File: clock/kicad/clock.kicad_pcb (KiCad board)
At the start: 2 copper layers, 152.9 x 74.9 mm, 75 parts, among them J1 USB-SS-52100-001, Q1 PN2222A, SW1 HOUR, SW2 MIN, SW3 TIME, U1 74HC4060, U10 74HC390, U11 NE555P, U12 74HC4511, U13 74HC4511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

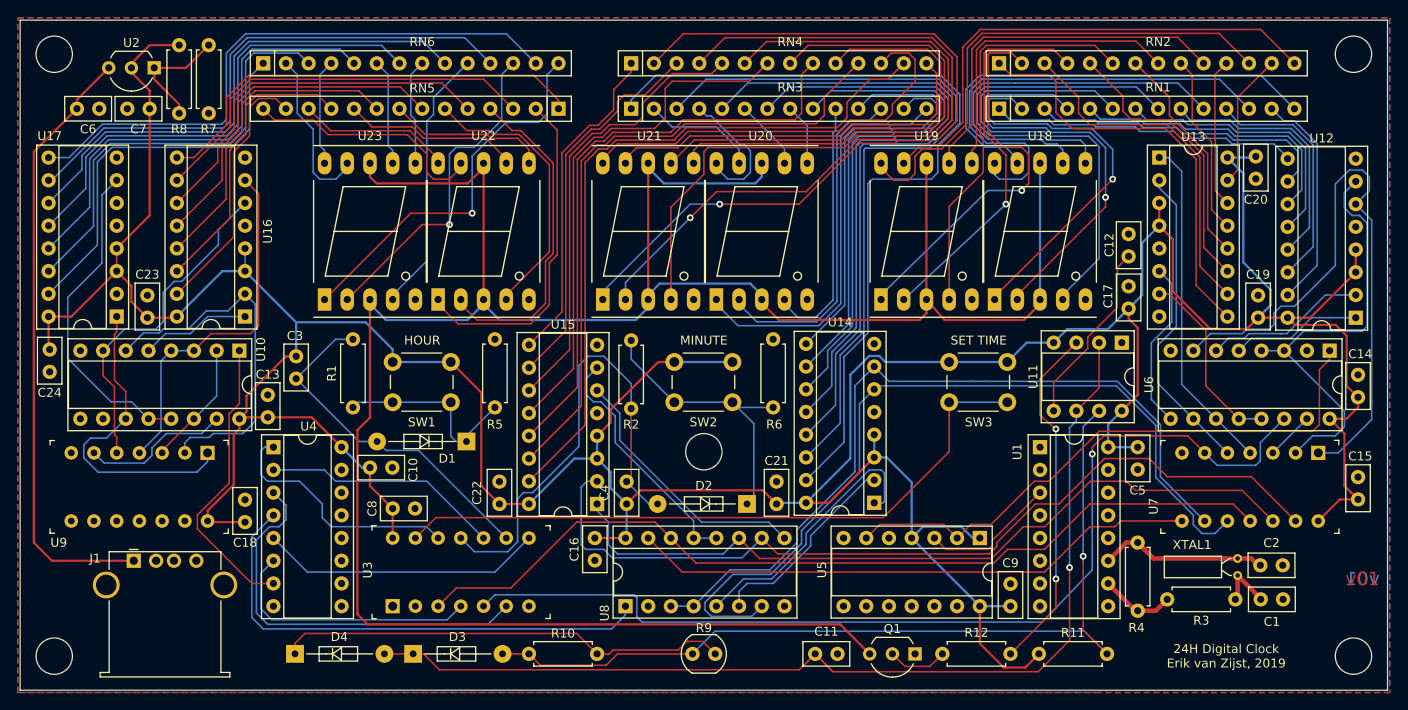
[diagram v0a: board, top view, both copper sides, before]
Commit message: Clock: Using a 500Ohm trimpot to tune the voltage regulator.
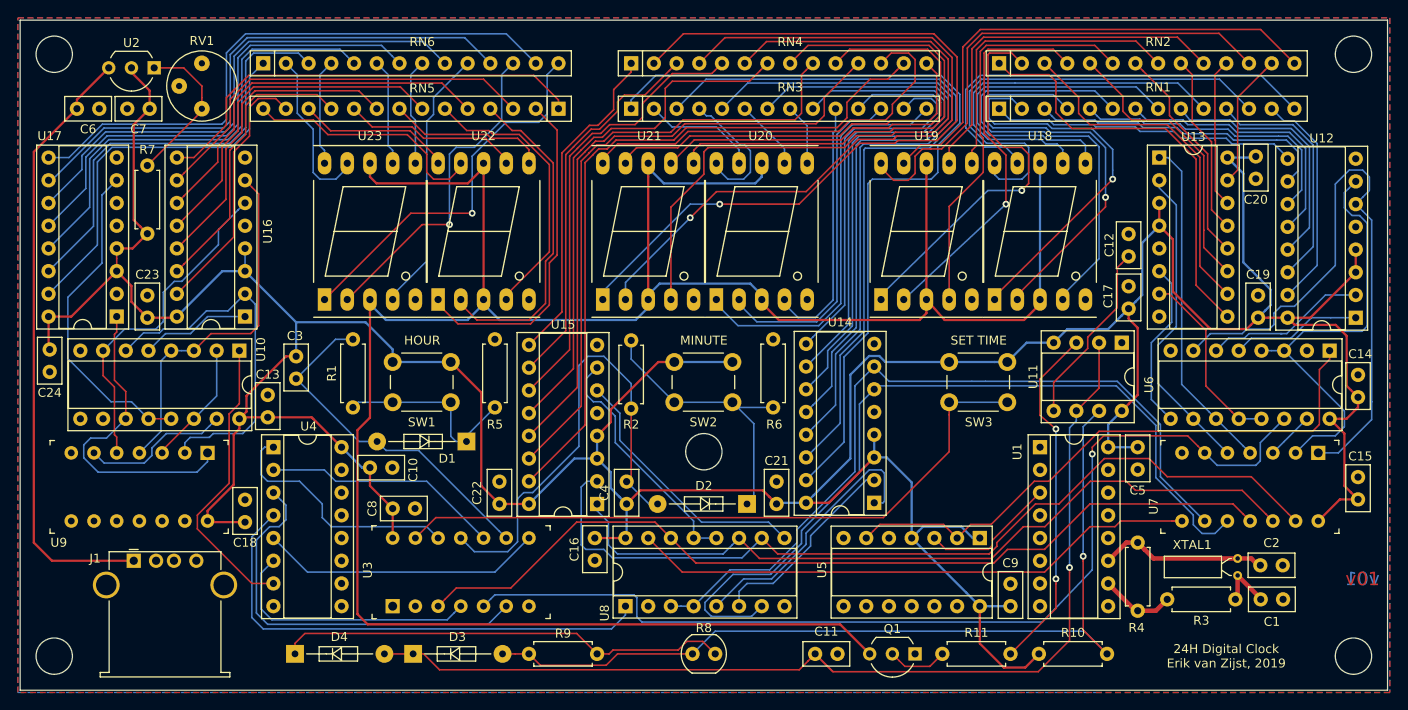
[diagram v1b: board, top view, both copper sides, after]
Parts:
- removed the R7 at (145.3, 59.9)
- added RV1: 0-500, Potentiometer_THT:Potentiometer_Bourns_3339P_Vertical_HandSoldering, F.Cu at (144.5, 67.1)
- moved R7 21.4 mm to (138.4, 81.0), turned to 90 degrees
- renumbered R11 to R10, R12 to R11, R8 to R7, R9 to R8, R10 to R9
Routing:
- net VCC: track 479.6 -> 475.2 mm
- net Net-(R7-Pad2): track 13.4 -> 17.6 mm

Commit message: Clock: Tweak PWM RC values.
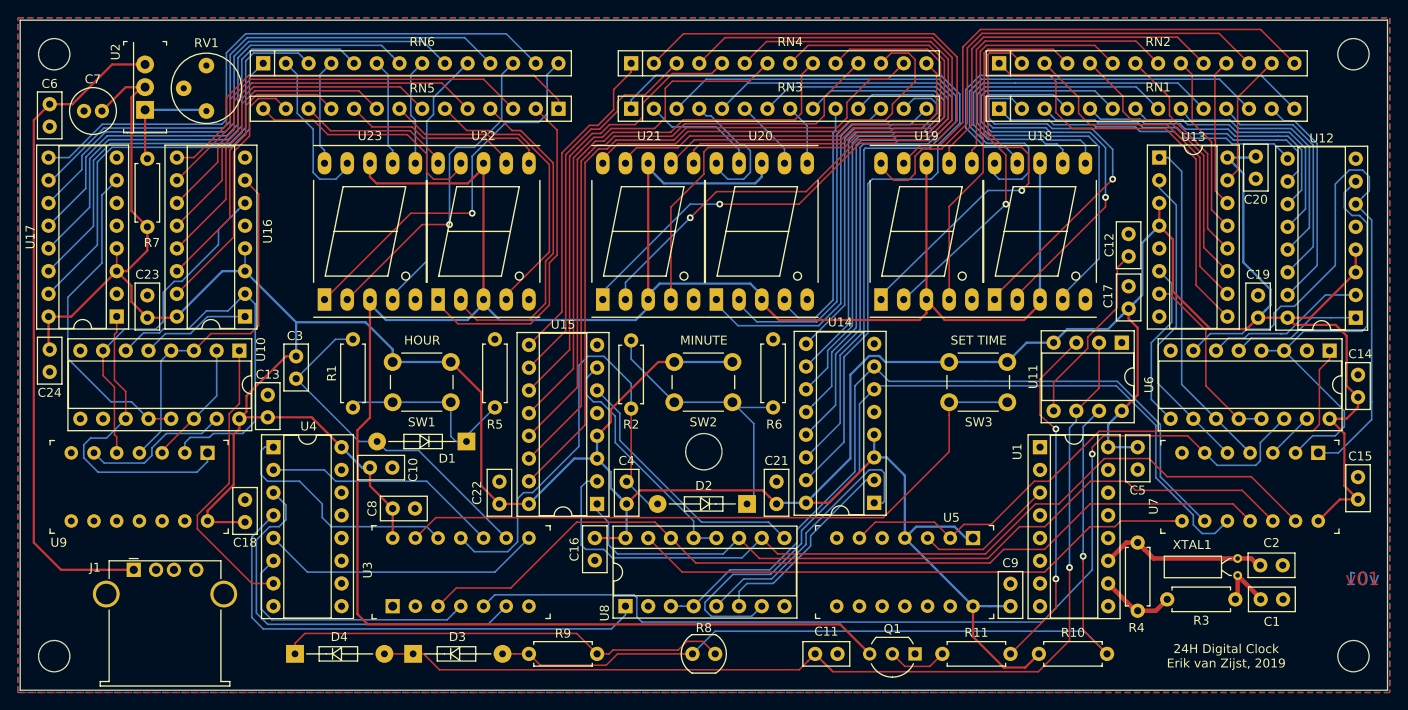
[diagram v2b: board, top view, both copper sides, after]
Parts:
- C7: footprint Capacitor_THT:C_Disc_D5.0mm_W2.5mm_P2.50mm -> Capacitor_THT:C_Radial_D5.0mm_H11.0mm_P2.00mm
- R7: value 120 -> 220
- U2: value LM317L_TO92 -> LD1117V; footprint Package_TO_SOT_THT:TO-92_Inline_Wide -> digikey-footprints:TO-220-3
- U5: footprint Package_DIP:DIP-14_W7.62mm_Socket -> clock:Socket_DIP-14_0.775in_Conn
- moved C7 5.34 mm to (133.3, 67.3)
- moved U2 4.81 mm to (138.2, 67.2), turned to 90 degrees
- moved C6 3.09 mm to (127.5, 66.5), turned to 270 degrees
- moved J1 1.02 mm to (136.9, 118.6)
- moved R7 0.76 mm to (138.4, 80.3)
- moved U5 0.76 mm to (230.8, 115.1)
- moved RV1 0.57 mm to (145.0, 67.3)
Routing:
- net /5V: track 68.6 -> 74.7 mm
- net VCC: track 475.2 -> 481.3 mm
- net Net-(R7-Pad2): track 17.6 -> 12.5 mm
- net Net-(U5-Pad2): track 65.9 -> 66.9 mm
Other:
- outline, holes or cut-outs redrawn

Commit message: Clock: Changed Resistor Networks to real parts.
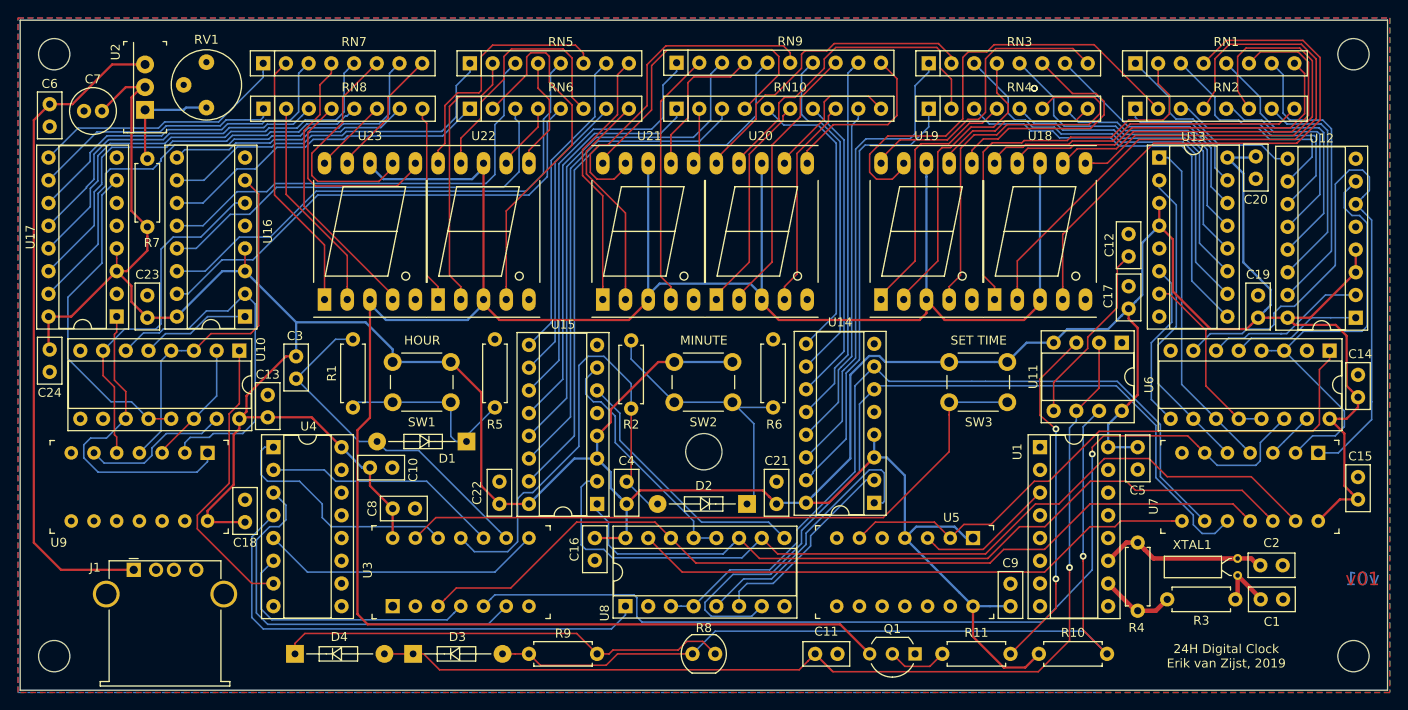
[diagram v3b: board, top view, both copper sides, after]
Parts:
- added RN10: R_Pack05_SIP, Resistor_THT:R_Array_SIP10, F.Cu at (197.6, 67.1)
- added RN7: R_Pack04_SIP, Resistor_THT:R_Array_SIP8, F.Cu at (151.4, 62.0)
- added RN8: R_Pack04_SIP, Resistor_THT:R_Array_SIP8, F.Cu at (151.4, 67.1)
- added RN9: R_Pack05_SIP, Resistor_THT:R_Array_SIP10, F.Cu at (197.6, 61.9)
- C11: value 100nF -> 47nF
- R10: value 1K -> 10K
- R11: value 100K -> 5.1K
- R9: value 100K -> 1M
- RN1, RN2, RN3, RN4, RN5, RN6: value 330 -> R_Pack04_SIP; footprint Resistor_THT:R_Array_SIP14 -> Resistor_THT:R_Array_SIP8
- moved RN3 33.7 mm to (225.8, 62.0)
- moved RN4 33.7 mm to (225.8, 67.1)
- moved RN6 23.7 mm to (174.5, 67.1)
- moved RN1 16.1 mm to (248.9, 62.0)
- moved RN2 16.1 mm to (248.9, 67.1)
- moved RN5 11.1 mm to (174.5, 62.0), turned to 0 degrees
- moved RV1 0.38 mm to (145.0, 66.9)
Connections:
- U12 pad 10: Net-(RN1-Pad3) -> Net-(RN2-Pad3)
- U12 pad 11: Net-(RN1-Pad5) -> Net-(RN1-Pad3)
- U12 pad 12: Net-(RN1-Pad7) -> Net-(RN2-Pad5)
- U12 pad 13: Net-(RN1-Pad9) -> Net-(RN1-Pad5)
- U12 pad 14: Net-(RN1-Pad11) -> Net-(RN2-Pad7)
- U12 pad 15: Net-(RN1-Pad13) -> Net-(RN1-Pad7)
- U13 pad 10: Net-(RN2-Pad3) -> Net-(RN3-Pad3)
- U13 pad 11: Net-(RN2-Pad5) -> Net-(RN4-Pad5)
- U13 pad 12: Net-(RN2-Pad7) -> Net-(RN3-Pad5)
- U13 pad 13: Net-(RN2-Pad9) -> Net-(RN4-Pad7)
- U13 pad 14: Net-(RN2-Pad11) -> Net-(RN3-Pad7)
- U13 pad 15: Net-(RN2-Pad13) -> Net-(RN2-Pad1)
- U13 pad 9: Net-(RN2-Pad1) -> Net-(RN4-Pad3)
- U14 pad 10: Net-(RN3-Pad11) -> Net-(RN9-Pad7)
- U14 pad 11: Net-(RN3-Pad9) -> Net-(RN10-Pad7)
- U14 pad 12: Net-(RN3-Pad7) -> Net-(RN9-Pad9)
- U14 pad 13: Net-(RN3-Pad5) -> Net-(RN10-Pad9)
- U14 pad 14: Net-(RN3-Pad3) -> Net-(RN3-Pad1)
- U14 pad 15: Net-(RN3-Pad1) -> Net-(RN4-Pad1)
- U14 pad 9: Net-(RN3-Pad13) -> Net-(RN10-Pad5)
- U15 pad 10: Net-(RN4-Pad3) -> Net-(RN6-Pad7)
- U15 pad 11: Net-(RN4-Pad5) -> Net-(RN9-Pad1)
- U15 pad 12: Net-(RN4-Pad7) -> Net-(RN10-Pad1)
- U15 pad 13: Net-(RN4-Pad9) -> Net-(RN9-Pad3)
- U15 pad 14: Net-(RN4-Pad11) -> Net-(RN10-Pad3)
- U15 pad 15: Net-(RN4-Pad13) -> Net-(RN9-Pad5)
- U15 pad 9: Net-(RN4-Pad1) -> Net-(RN5-Pad7)
- U16 pad 10: Net-(RN5-Pad3) -> Net-(RN5-Pad1)
- U16 pad 11: Net-(RN5-Pad5) -> Net-(RN6-Pad1)
- U16 pad 12: Net-(RN5-Pad7) -> Net-(RN5-Pad3)
- U16 pad 13: Net-(RN5-Pad9) -> Net-(RN6-Pad3)
- U16 pad 14: Net-(RN5-Pad11) -> Net-(RN5-Pad5)
- U16 pad 15: Net-(RN5-Pad13) -> Net-(RN6-Pad5)
- U16 pad 9: Net-(RN5-Pad1) -> Net-(RN8-Pad7)
- U17 pad 10: Net-(RN6-Pad11) -> Net-(RN8-Pad1)
- U17 pad 11: Net-(RN6-Pad9) -> Net-(RN7-Pad3)
- U17 pad 12: Net-(RN6-Pad7) -> Net-(RN8-Pad3)
- U17 pad 13: Net-(RN6-Pad5) -> Net-(RN7-Pad5)
- U17 pad 14: Net-(RN6-Pad3) -> Net-(RN8-Pad5)
- U17 pad 15: Net-(RN6-Pad1) -> Net-(RN7-Pad7)
- U17 pad 9: Net-(RN6-Pad13) -> Net-(RN7-Pad1)
- U18 pad 10: Net-(RN1-Pad12) -> Net-(RN2-Pad8)
- U18 pad 2: Net-(RN1-Pad4) -> Net-(RN2-Pad4)
- U18 pad 4: Net-(RN1-Pad6) -> Net-(RN1-Pad4)
- U18 pad 6: Net-(RN1-Pad8) -> Net-(RN2-Pad6)
- U18 pad 7: Net-(RN1-Pad10) -> Net-(RN1-Pad6)
- U18 pad 9: Net-(RN1-Pad14) -> Net-(RN1-Pad8)
- U19 pad 1: Net-(RN2-Pad2) -> Net-(RN4-Pad4)
- U19 pad 10: Net-(RN2-Pad12) -> Net-(RN3-Pad8)
- U19 pad 2: Net-(RN2-Pad4) -> Net-(RN3-Pad4)
- U19 pad 4: Net-(RN2-Pad6) -> Net-(RN4-Pad6)
- U19 pad 6: Net-(RN2-Pad8) -> Net-(RN3-Pad6)
- U19 pad 7: Net-(RN2-Pad10) -> Net-(RN4-Pad8)
- U19 pad 9: Net-(RN2-Pad14) -> Net-(RN2-Pad2)
- U20 pad 1: Net-(RN3-Pad14) -> Net-(RN10-Pad6)
- U20 pad 10: Net-(RN3-Pad4) -> Net-(RN3-Pad2)
- U20 pad 2: Net-(RN3-Pad12) -> Net-(RN9-Pad8)
- U20 pad 4: Net-(RN3-Pad10) -> Net-(RN10-Pad8)
- U20 pad 6: Net-(RN3-Pad8) -> Net-(RN9-Pad10)
- U20 pad 7: Net-(RN3-Pad6) -> Net-(RN10-Pad10)
- U20 pad 9: Net-(RN3-Pad2) -> Net-(RN4-Pad2)
- U21 pad 1: Net-(RN4-Pad2) -> Net-(RN5-Pad8)
- U21 pad 10: Net-(RN4-Pad12) -> Net-(RN10-Pad4)
- U21 pad 2: Net-(RN4-Pad4) -> Net-(RN6-Pad8)
- U21 pad 4: Net-(RN4-Pad6) -> Net-(RN9-Pad2)
- U21 pad 6: Net-(RN4-Pad8) -> Net-(RN10-Pad2)
- U21 pad 7: Net-(RN4-Pad10) -> Net-(RN9-Pad4)
- U21 pad 9: Net-(RN4-Pad14) -> Net-(RN9-Pad6)
- U22 pad 1: Net-(RN5-Pad2) -> Net-(RN8-Pad8)
- U22 pad 10: Net-(RN5-Pad12) -> Net-(RN5-Pad6)
- U22 pad 2: Net-(RN5-Pad4) -> Net-(RN5-Pad2)
- U22 pad 4: Net-(RN5-Pad6) -> Net-(RN6-Pad2)
- U22 pad 6: Net-(RN5-Pad8) -> Net-(RN5-Pad4)
- U22 pad 7: Net-(RN5-Pad10) -> Net-(RN6-Pad4)
- U22 pad 9: Net-(RN5-Pad14) -> Net-(RN6-Pad6)
- U23 pad 1: Net-(RN6-Pad14) -> Net-(RN7-Pad2)
- U23 pad 10: Net-(RN6-Pad4) -> Net-(RN8-Pad6)
- U23 pad 2: Net-(RN6-Pad12) -> Net-(RN8-Pad2)
- U23 pad 4: Net-(RN6-Pad10) -> Net-(RN7-Pad4)
- U23 pad 6: Net-(RN6-Pad8) -> Net-(RN8-Pad4)
- U23 pad 7: Net-(RN6-Pad6) -> Net-(RN7-Pad6)
- U23 pad 9: Net-(RN6-Pad2) -> Net-(RN7-Pad8)
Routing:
- net Net-(RN4-Pad13): track 79.5 -> 0.00 mm
- net Net-(RN4-Pad11): track 72.4 -> 0.00 mm
- net Net-(RN4-Pad9): track 66.5 -> 0.00 mm
- net Net-(RN9-Pad5): track 0.00 -> 66.2 mm
- net Net-(RN6-Pad13): track 65.9 -> 0.00 mm
- net Net-(RN6-Pad11): track 61.6 -> 0.00 mm
- net Net-(RN3-Pad9): track 59.0 -> 0.00 mm
- net Net-(RN6-Pad9): track 58.1 -> 0.00 mm
- net Net-(RN9-Pad3): track 0.00 -> 57.0 mm
- net Net-(RN7-Pad7): track 0.00 -> 56.8 mm
- net Net-(RN2-Pad12): track 56.5 -> 0.00 mm
- net Net-(RN2-Pad14): track 56.5 -> 0.00 mm
- net Net-(RN4-Pad2): track 91.9 -> 37.0 mm, vias 1 -> 0
- net Net-(RN10-Pad3): track 0.00 -> 54.7 mm
- net Net-(RN4-Pad4): track 83.3 -> 29.4 mm, vias 1 -> 0
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
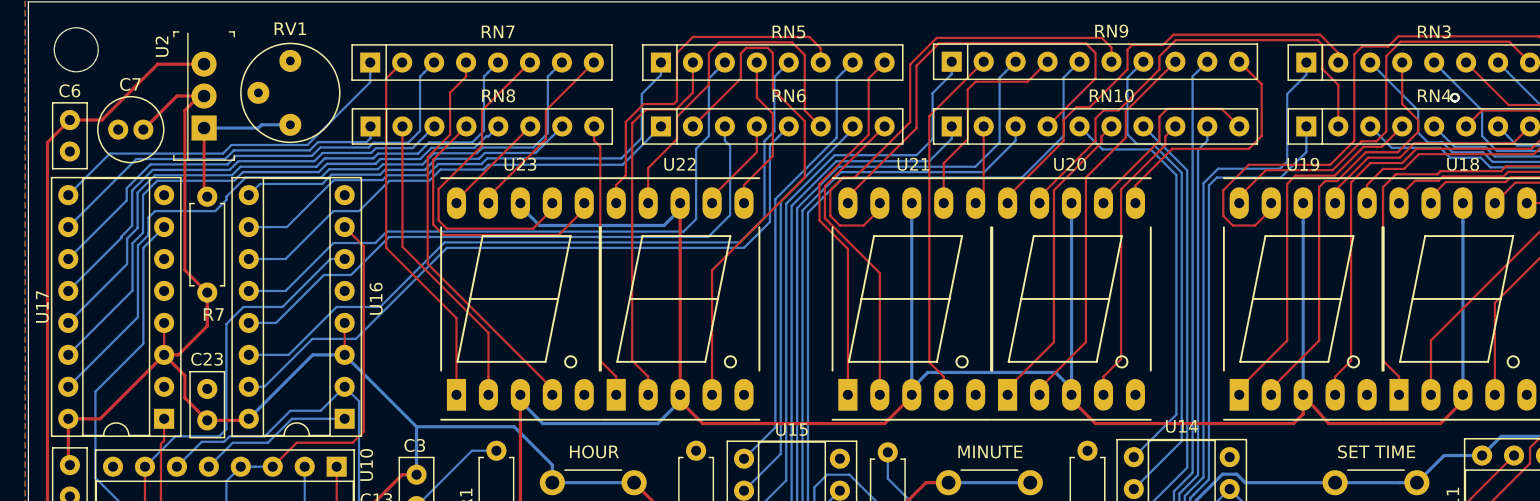
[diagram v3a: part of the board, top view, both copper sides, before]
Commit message: Clock: Added Bill Of Materials.
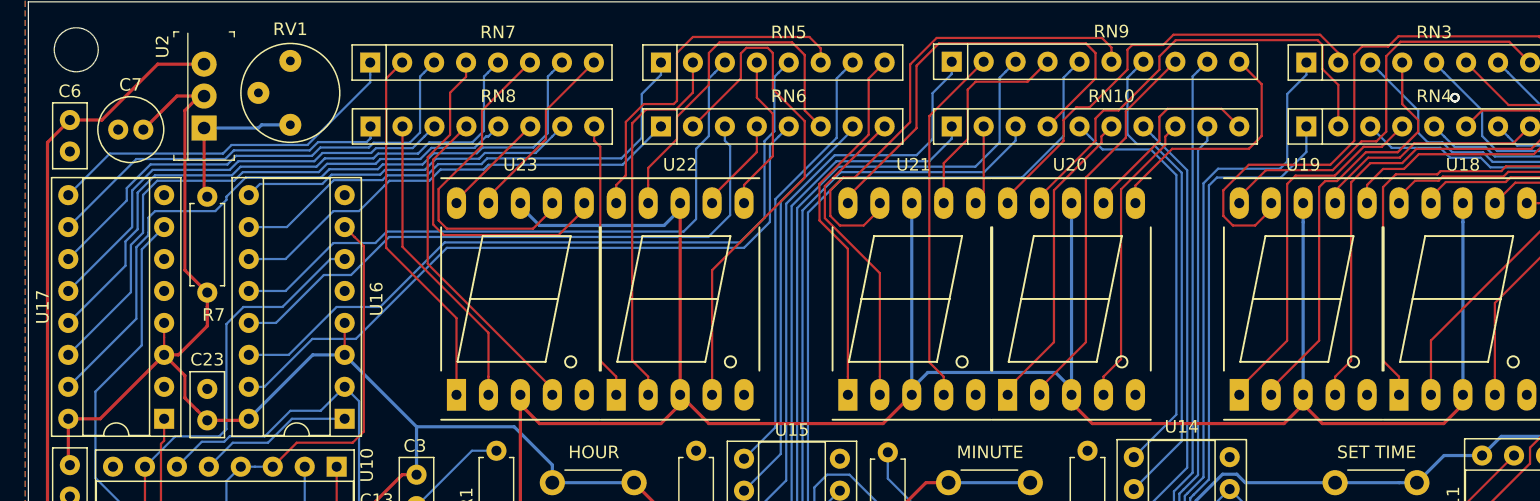
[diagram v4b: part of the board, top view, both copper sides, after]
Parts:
- C1, C2: value 20pF -> 22pF
- C6: value 10uF -> 100nF
- R3: value 470k -> 330k
- R7: value 220 -> 220R
- RN1, RN2, RN3, RN4, RN5, RN6, RN7, RN8: value R_Pack04_SIP -> 150R
- RN10, RN9: value R_Pack05_SIP -> 150R
- RV1: value 0-500 -> 500R
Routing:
- net Net-(Q1-Pad3): track 273.2 -> 272.1 mm
